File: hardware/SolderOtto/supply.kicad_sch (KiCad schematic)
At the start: 78 parts, among them J201 Conn_02x04_Counter_Clockwise, Q201 T2N7002AK, Q202 BC858B, Q203 BC847A, Q204 BC847A, U201 LM5012, U202 AP3211K, U203 AP3211K, U204 AP3211K, U205 LM27761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

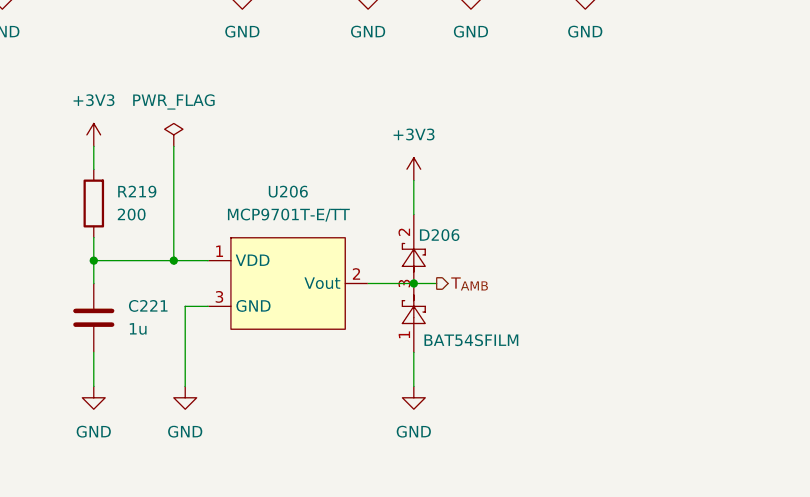
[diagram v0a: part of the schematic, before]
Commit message: try to replace op07c
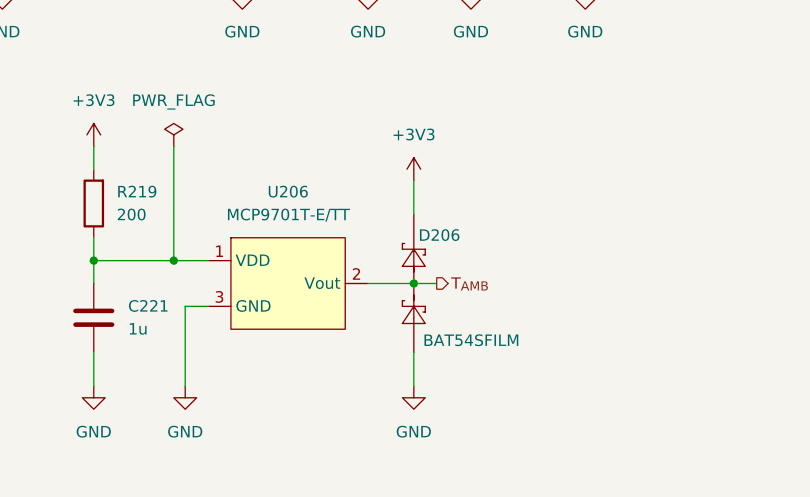
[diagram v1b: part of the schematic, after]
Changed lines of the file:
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@@
 	)
 	(symbol
-		(lib_name "BAT54SFILM_1")
 		(lib_id "mylib_diodes:BAT54SFILM")
 		(at 101.6 173.99 90)

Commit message: fix some part numbers
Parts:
- D206, D207: Mouser 511-BAT54SFILM -> (none)
- JS201: Digikey 668-SMI-1027-T-5V-RDKR-ND -> 668-SMI-1027-T-5V-RCT-ND
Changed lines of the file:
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@@
 			)
 		)
-		(property "Mouser" "511-BAT54SFILM"
-			(at 165.354 182.118 90)
-			(effects
-				(font
-					(size 1.27 1.27)
-				)
-				(justify right)
-				(hide yes)
-			)
-		)
 		(property "Digikey" "497-2522-1-ND"
 			(at 163.83 172.72 0)
@@
 			)
 		)
-		(property "Mouser" "511-BAT54SFILM"
-			(at 108.712 178.308 0)
-			(effects
-				(font
-					(size 1.27 1.27)
-				)
-				(hide yes)
-			)
-		)
 		(pin "3"
 		)
@@
 			)
 		)
-		(property "Digikey" "668-SMI-1027-T-5V-RDKR-ND"
+		(property "Digikey" "668-SMI-1027-T-5V-RCT-ND"
 			(at 266.7 125.7299 0)
 			(effects

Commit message: remove low side switching ic
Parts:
- U206: value MCP9701T-E/TT -> MCP9701T-E/TT
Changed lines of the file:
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@@
 			)
 		)
-		(property "Value" " MCP9701T-E/TT"
+		(property "Value" "MCP9701T-E/TT"
 			(at 149.86 165.1 0)
 			(effects

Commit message: rework pcb due to not working one
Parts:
- C203, C206: footprint Capacitor_SMD:CP_Elec_6.3x5.7 -> Capacitor_SMD:CP_Elec_10x10
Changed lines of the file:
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@@
 			)
 		)
-		(property "Footprint" "Capacitor_SMD:CP_Elec_6.3x5.7"
+		(property "Footprint" "Capacitor_SMD:CP_Elec_10x10"
 			(at 276.5552 36.83 0)
 			(effects
@@
 			)
 		)
-		(property "Footprint" "Capacitor_SMD:CP_Elec_6.3x5.7"
+		(property "Footprint" "Capacitor_SMD:CP_Elec_10x10"
 			(at 154.6352 35.56 0)
 			(effects

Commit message: rework some shit
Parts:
- added J202: Conn_02x04_Counter_Clockwise, Connector_Molex:Molex_Nano-Fit_105310-xx10_2x05_P2.50mm_Vertical, symbol Connector_Generic:Conn_02x04_Top_Bottom
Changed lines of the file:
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@@
+	)
+	(symbol
+		(lib_id "Connector_Generic:Conn_02x04_Top_Bottom")
+		(at 68.58 29.21 90)
+		(mirror x)
+		(unit 1)
+		(exclude_from_sim yes)
+		(in_bom yes)
+		(on_board yes)
+		(dnp no)
+		(property "Reference" "J202"
+			(at 63.754 31.75 0)
+			(effects
+				(font
+					(size 1.27 1.27)
+				)
+				(justify right)
+			)
+		)
+		(property "Value" "Conn_02x04_Counter_Clockwise"
+			(at 76.2 31.7499 90)
+			(effects
+				(font
+					(size 1.27 1.27)
+				)
+				(justify right)
+				(hide yes)
+			)
+		)
+		(property "Footprint" "Connector_Molex:Molex_Nano-Fit_105310-xx10_2x05_P2.50mm_Vertical"
+			(at 68.58 29.21 0)
+			(effects
+				(font
+					(size 1.27 1.27)
+				)
+				(hide yes)
+			)
+		)
+		(property "Datasheet" "~"
+			(at 68.58 29.21 0)
+			(effects
+				(font
+					(size 1.27 1.27)
+				)
+				(hide yes)
+			)
+		)
+		(property "Description" "Generic connector, double row, 02x04, top/bottom pin numbering scheme (row 1: 1...pins_per_row, row2: pins_per_row+1 ... num_pins), script generated (kicad-library-utils/schlib/autogen/connector/)"
+			(at 68.58 29.21 0)
+			(effects
+				(font
+					(size 1.27 1.27)
+				)
+				(hide yes)
+			)
+		)
+		(property "Digikey" "WM17932-ND"
+			(at 68.58 29.21 0)
+			(effects
+				(font
+					(size 1.27 1.27)
+				)
+				(hide yes)
+			)
+		)
+		(pin "6"
+		)
+		(pin "8"
+		)
+		(pin "2"
+		)
+		(pin "1"
+		)
+		(pin "5"
+		)
+		(pin "3"
+		)
+		(pin "4"
+		)
+		(pin "7"
+		)
+		(instances
+			(project "SolderOtto"
+				(path "/04e99464-bf33-4a4f-8397-d26b5ec904f3/1f74b07f-4a28-48ba-be90-ad5de8d466f3"
+					(reference "J202")
+					(unit 1)
+				)
+			)
+		)
 	)
 	(symbol

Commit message: rework pcb
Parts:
- removed J202: Conn_02x04_Counter_Clockwise, Connector_Molex:Molex_Nano-Fit_105310-xx10_2x05_P2.50mm_Vertical, symbol Connector_Generic:Conn_02x04_Top_Bottom
- C203, C206: value 22u -> 100u; footprint Capacitor_SMD:CP_Elec_10x10 -> mylib_common:CP_Elec_10x10.5_A768; Digikey 399-A768EB226M1HLAE048CT-ND -> 399-A768MS107M1HLAE024CT-ND
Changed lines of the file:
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@@
 			)
 		)
-		(property "Value" "22u"
+		(property "Value" "100u"
 			(at 279.4 33.4009 0)
 			(effects
@@
 			)
 		)
-		(property "Footprint" "Capacitor_SMD:CP_Elec_10x10"
+		(property "Footprint" "mylib_common:CP_Elec_10x10.5_A768"
 			(at 276.5552 36.83 0)
 			(effects
@@
 			)
 		)
-		(property "Digikey" "399-A768EB226M1HLAE048CT-ND"
+		(property "Digikey" "399-A768MS107M1HLAE024CT-ND"
 			(at 275.59 33.02 0)
 			(effects
@@
 	)
 	(symbol
-		(lib_id "Connector_Generic:Conn_02x04_Top_Bottom")
-		(at 68.58 29.21 90)
-		(mirror x)
-		(unit 1)
-		(exclude_from_sim yes)
-		(in_bom yes)
-		(on_board yes)
-		(dnp no)
-		(property "Reference" "J202"
-			(at 63.754 31.75 0)
-			(effects
-				(font
-					(size 1.27 1.27)
-				)
-				(justify right)
-			)
-		)
-		(property "Value" "Conn_02x04_Counter_Clockwise"
-			(at 76.2 31.7499 90)
-			(effects
-				(font
-					(size 1.27 1.27)
-				)
-				(justify right)
-				(hide yes)
-			)
-		)
-		(property "Footprint" "Connector_Molex:Molex_Nano-Fit_105310-xx10_2x05_P2.50mm_Vertical"
-			(at 68.58 29.21 0)
-			(effects
-				(font
-					(size 1.27 1.27)
-				)
-				(hide yes)
-			)
-		)
-		(property "Datasheet" "~"
-			(at 68.58 29.21 0)
-			(effects
-				(font
-					(size 1.27 1.27)
-				)
-				(hide yes)
-			)
-		)
-		(property "Description" "Generic connector, double row, 02x04, top/bottom pin numbering scheme (row 1: 1...pins_per_row, row2: pins_per_row+1 ... num_pins), script generated (kicad-library-utils/schlib/autogen/connector/)"
-			(at 68.58 29.21 0)
-			(effects
-				(font
-					(size 1.27 1.27)
-				)
-				(hide yes)
-			)
-		)
-		(property "Digikey" "WM17932-ND"
-			(at 68.58 29.21 0)
-			(effects
-				(font
-					(size 1.27 1.27)
-				)
-				(hide yes)
-			)
-		)
-		(pin "6"
-		)
-		(pin "8"
-		)
-		(pin "2"
-		)
-		(pin "1"
-		)
-		(pin "5"
-		)
-		(pin "3"
-		)
-		(pin "4"
-		)
-		(pin "7"
-		)
-		(instances
-			(project "SolderOtto"
-				(path "/04e99464-bf33-4a4f-8397-d26b5ec904f3/1f74b07f-4a28-48ba-be90-ad5de8d466f3"
-					(reference "J202")
-					(unit 1)
-				)
-			)
-		)
-	)
-	(symbol
 		(lib_id "power:GND")
 		(at 19.05 83.82 0)
@@
 			)
 		)
-		(property "Value" "22u"
+		(property "Value" "100u"
 			(at 157.48 32.1309 0)
 			(effects
@@
 			)
 		)
-		(property "Footprint" "Capacitor_SMD:CP_Elec_10x10"
+		(property "Footprint" "mylib_common:CP_Elec_10x10.5_A768"
 			(at 154.6352 35.56 0)
 			(effects
@@
 			)
 		)
-		(property "Digikey" "399-A768EB226M1HLAE048CT-ND"
+		(property "Digikey" "399-A768MS107M1HLAE024CT-ND"
 			(at 153.67 31.75 0)
 			(effects

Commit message: change some parts
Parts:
- C219: value 10u -> 2u2; Digikey 1276-2891-1-ND -> (none)
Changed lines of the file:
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@@
 			)
 		)
-		(property "Value" "10u"
+		(property "Value" "2u2"
 			(at 186.69 129.5399 0)
 			(effects
@@
 			)
 		)
-		(property "Digikey" "1276-2891-1-ND"
+		(property "Digikey" ""
 			(at 182.88 128.27 0)
 			(effects

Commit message: start rework supplies
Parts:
- removed C208, C209, C210: 10n, Capacitor_SMD:C_0603_1608Metric, symbol Device:C
- removed C211, C212, C213: 10u, Capacitor_SMD:C_0805_2012Metric, symbol Device:C
- removed C214, C215, C216: 22u, Capacitor_SMD:C_0805_2012Metric, symbol Device:C
- removed C217, C220: 4u7, Capacitor_SMD:C_0603_1608Metric, symbol Device:C
- removed C218: 1u, Capacitor_SMD:C_0603_1608Metric, symbol Device:C
- removed C219: 2u2, Capacitor_SMD:C_0805_2012Metric, symbol Device:C
- removed D204, D205: SMD16PL-TP, Diode_SMD:D_SOD-123F, symbol Device:D_Schottky
- removed L202: 1u5, Inductor_SMD:L_Taiyo-Yuden_NR-40xx, symbol Device:L
- removed L203, L204: 3u3, Inductor_SMD:L_Taiyo-Yuden_NR-40xx, symbol Device:L
- removed R209: 9k53, Resistor_SMD:R_0603_1608Metric, symbol Device:R
- removed R210: 16k2, Resistor_SMD:R_0603_1608Metric, symbol Device:R
- removed R211: 215k, Resistor_SMD:R_0603_1608Metric, symbol Device:R
- removed R213: 69k, Resistor_SMD:R_0603_1608Metric, symbol Device:R
- removed TP204: 8V, TestPoint:TestPoint_Keystone_5015_Micro-Minature, symbol Connector:TestPoint
- removed TP205: 5V, TestPoint:TestPoint_Keystone_5015_Micro-Minature, symbol Connector:TestPoint
- removed TP206: 3V3, TestPoint:TestPoint_Keystone_5015_Micro-Minature, symbol Connector:TestPoint
- removed U202, U203, U204: AP3211K, Package_TO_SOT_SMD:SOT-23-6, symbol Regulator_Switching:AP3211K
- removed U205: LM27761, Package_SON:WSON-8-1EP_2x2mm_P0.5mm_EP0.9x1.6mm, symbol Regulator_SwitchedCapacitor:LM27761
- added C208, C209: 100u, mylib_common:CP_Elec_10x10.5_A768, symbol Device:C_Polarized
- added U202: LM337_TO252, Package_TO_SOT_SMD:TO-252-2, symbol Regulator_Linear:LM337_TO252
- added U203: LM317_TO-252, Package_TO_SOT_SMD:TO-252-2, symbol Regulator_Linear:LM317_TO-252
- D203: value SMD16PL-TP -> STPS2H100A; footprint Diode_SMD:D_SOD-123F -> Diode_SMD:D_SMA; Digikey SMD16PL-TPMSCT-ND -> 497-3758-1-ND
- R204: value 49k9 -> 79k9; Digikey RMCF0603FT49K9CT-ND -> (none)
- R205: value 49k9 -> 200; Digikey RMCF0603FT49K9CT-ND -> (none)
- R206, R207: value 49k9 -> 120; Digikey RMCF0603FT49K9CT-ND -> (none)
- R208: value 5k62 -> 200; Digikey 311-5.62KHRCT-ND -> (none)
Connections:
- net +12V is gone; now on net +8V: C201.2, C206.1, L201.2, R202.1, TP202.1
- net +3V3: no longer R207.1
- net +5V: now also R206.2, U203.2 (VO); no longer R206.1
- net +8V: no longer R205.1
- net -5V: now also R207.1, C209.2, U202.3 (VO)
- net 24V_{AC}: now also D203.1 (K)
- net GND: now also R205.1, C208.1, C209.1; no longer D203.2 (A)
- net at R207.2: now also R208.1, U202.1 (ADJ)
- net at C203.1, C204.1, C205.1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: now also U203.3 (VI)
- net at R205.2: now also R206.1, U203.1 (ADJ); no longer R208.1
- new net: C208.2, D203.2 (A), U202.2 (VI)
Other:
- moved on the sheet: C201, C202, C203, C204, C205, C206, C207, D201, D202, L201, R201, R202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
